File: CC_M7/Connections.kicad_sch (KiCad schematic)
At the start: 12 parts, among them J1 Conn_01x04_Pin, J10 Conn_01x04_Pin, J11 USB_B_Micro, J12 Conn_01x04_Pin, J3 Conn_01x03_Pin, J4 Conn_01x03_Pin, J5 Conn_01x03_Pin, J6 Conn_01x03_Pin, J7 Conn_01x03_Pin, J8 Conn_01x03_Pin

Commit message: last control
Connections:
- net GND: no longer J2.34 (Pin_34)
- net J2_38: no longer names the net of J2.38 (Pin_38)
- net PE5 renamed J2_31
- net PE6: no longer names the net of J2.29 (Pin_29)
- new net J2_34: J2.34 (Pin_34)
- no-connect marks 4 -> 6
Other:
- moved on the sheet: J10, J11, J12, J2, J3, J4, J5, J6, J7, J8, R7

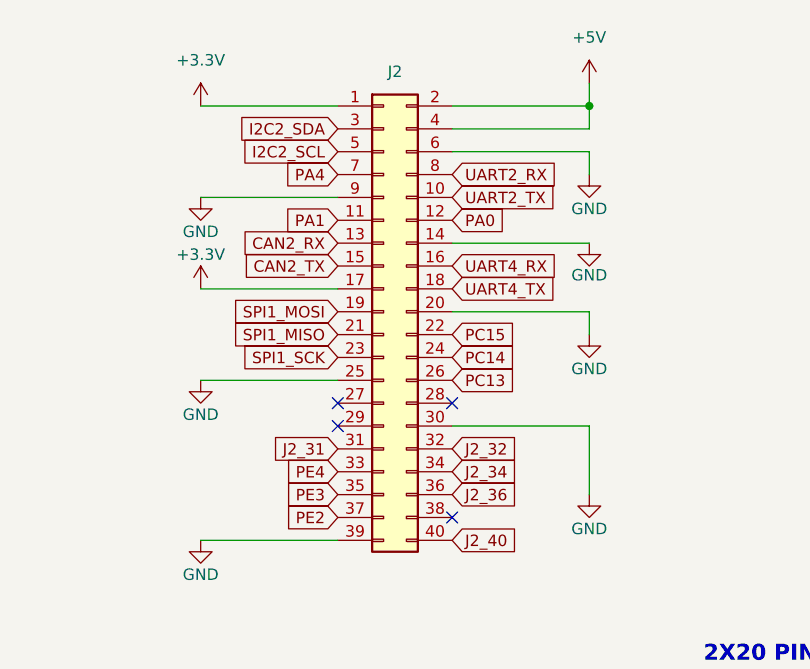
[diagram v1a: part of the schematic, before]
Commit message: ready to routing
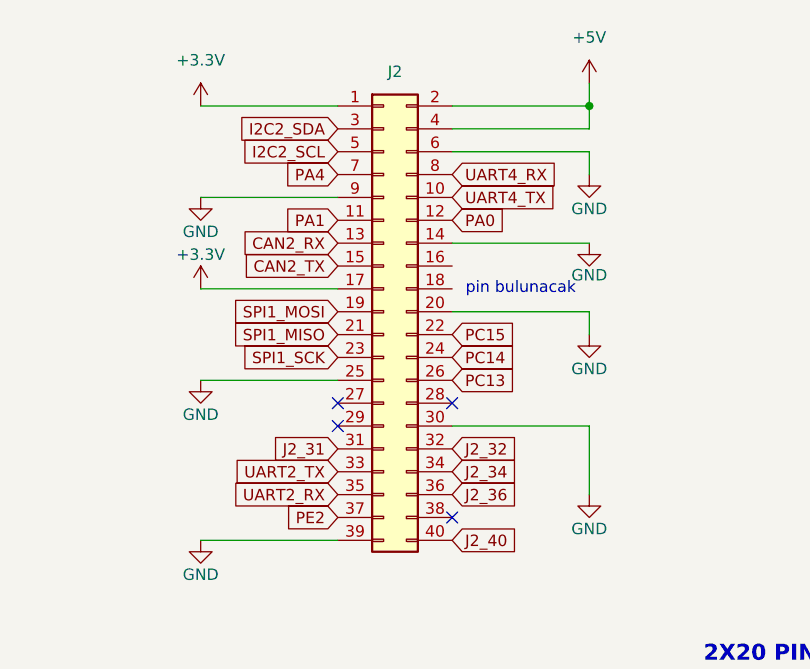
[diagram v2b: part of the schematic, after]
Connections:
- net PE3 is gone; now on net UART2_RX: J2.35 (Pin_35)
- net PE4 is gone; now on net UART2_TX: J2.33 (Pin_33)
- net UART2_RX: no longer J2.8 (Pin_8)
- net UART2_TX: no longer J2.10 (Pin_10)
- net UART4_RX: now also J2.8 (Pin_8); no longer J2.16 (Pin_16)
- net UART4_TX: now also J2.10 (Pin_10); no longer J2.18 (Pin_18)
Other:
- note added: "pin bulunacak"

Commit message: last check
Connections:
- net USB_DM renamed USB_DN
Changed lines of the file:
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@@
 		)
 	)
-	(global_label "USB_DM"
+	(global_label "USB_DN"
 		(shape input)
 		(at 63.5 116.84 0)
@@
 		)
 		(property "Intersheetrefs" "${INTERSHEET_REFS}"
-			(at 73.9842 116.84 0)
+			(at 73.8633 116.84 0)
 			(effects
 				(font

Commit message: pdf added
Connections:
- no-connect marks 6 -> 8
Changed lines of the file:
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@@
+	)
+	(no_connect
+		(at 63.5 50.8)
 	)
 	(no_connect
@@
 	)
 	(no_connect
+		(at 63.5 48.26)
+	)
+	(no_connect
